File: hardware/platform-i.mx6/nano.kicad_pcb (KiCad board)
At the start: 4 copper layers, 85 x 56 mm, 196 parts, among them J1 SD-104031, J10 TC2030-IDC, J11 Conn_01x05, J2 TAG_CONNECT_JTAG, J3 TC2030-IDC, J4 USB_C_Receptacle_USB2.0, J5 CAN, J6 UART5, J7 I2C4, J8 ECSPI4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

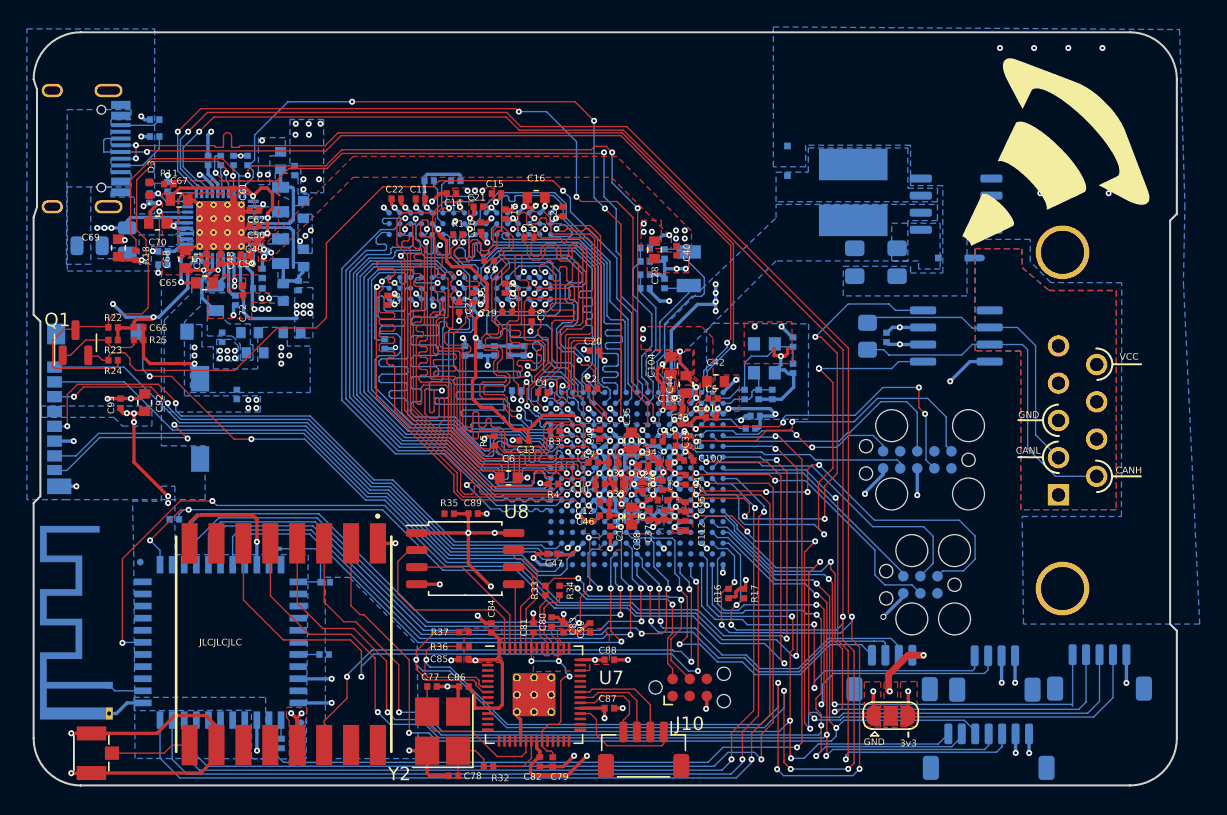
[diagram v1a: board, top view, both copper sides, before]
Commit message: Start reworking imx board into the new form factor
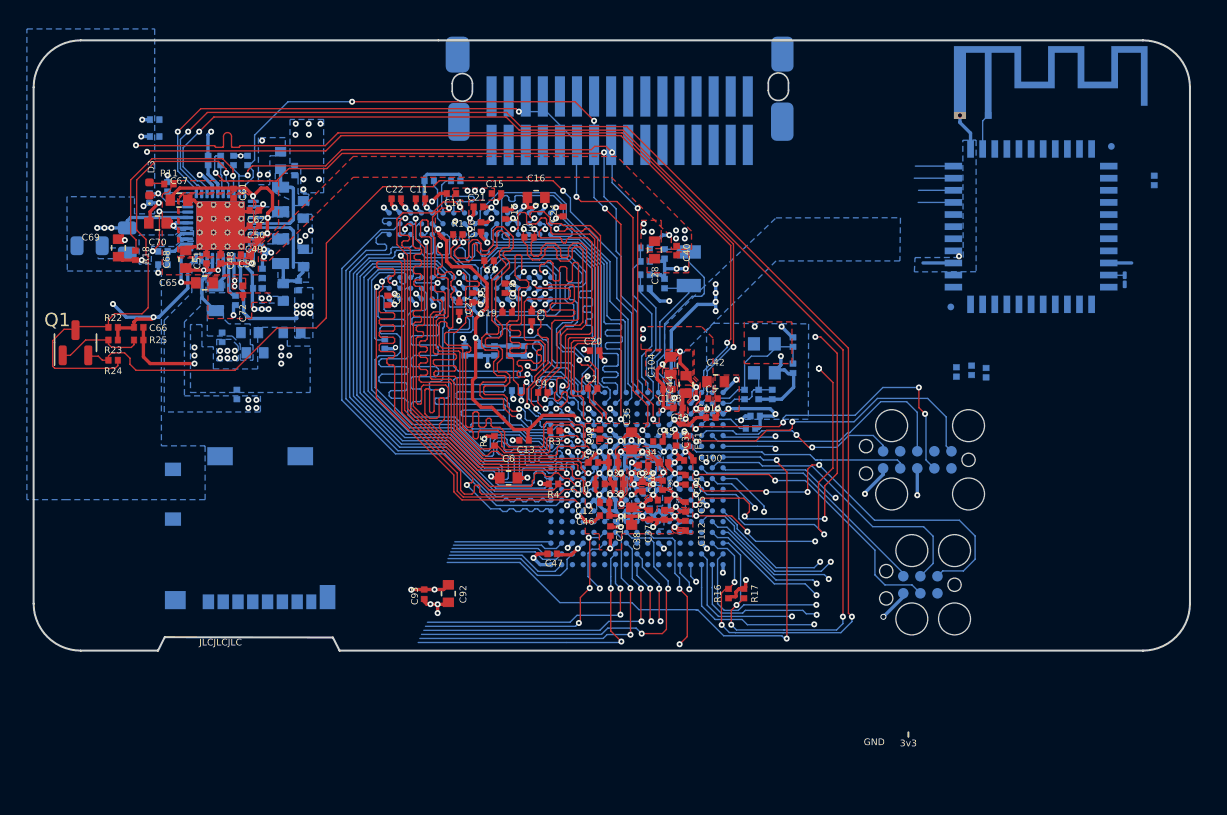
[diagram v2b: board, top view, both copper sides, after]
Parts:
- removed AE1: U.FL-R-SMT-1(10), ufl:HRS_U.FL-R-SMT-1(10)
- removed C73: 0.22uF, Custom Components:C_0402_narrow
- removed C75, C76: 10uF, Capacitor_SMD:C_0805_2012Metric_Pad1.18x1.45mm_HandSolder
- removed C77, C78: 10pF, Custom Components:C_0402_narrow
- removed C79, C81, C89: 1uF, Custom Components:C_0402_narrow
- removed C80, C82, C83, C84, C85, C86, C87, C88, C90: 0.1uF, Custom Components:C_0402_narrow
- removed D1, D2: D_Small, Diode_SMD:D_SOD-323F
- removed G***: LOGO, logos:cone
- removed J10: TC2030-IDC, Connector:Tag-Connect_TC2030-IDC-NL_2x03_P1.27mm_Vertical
- removed J11: Conn_01x05, Connector_JST:JST_SH_BM04B-SRSS-TB_1x04-1MP_P1.00mm_Vertical
- removed J4: USB_C_Receptacle_USB2.0, Connector_USB:USB_C_Receptacle_HRO_TYPE-C-31-M-12
- removed J5: CAN, Connector_Dsub:DSUB-9_Female_Horizontal_P2.77x2.84mm_EdgePinOffset4.94mm_Housed_MountingHolesOffset7.48mm
- removed J6: UART5, Connector_JST:JST_SH_BM05B-SRSS-TB_1x05-1MP_P1.00mm_Vertical
- removed J7: I2C4, Connector_JST:JST_SH_BM04B-SRSS-TB_1x04-1MP_P1.00mm_Vertical
- removed J8: ECSPI4, Connector_JST:JST_SH_BM07B-SRSS-TB_1x07-1MP_P1.00mm_Vertical
- removed J9: PWM, Connector_JST:JST_SH_BM04B-SRSS-TB_1x04-1MP_P1.00mm_Vertical
- removed JP1: IO_SW, Jumper:SolderJumper-3_P1.3mm_Open_RoundedPad1.0x1.5mm
- removed L5: 6.8uH, Inductor_SMD:L_Bourns_SRN6045TA
- removed R31: 120, Resistor_SMD:R_0805_2012Metric_Pad1.20x1.40mm_HandSolder
- removed R32, R35, R36, R37: 1k, Custom Components:R_0402_narrow
- removed R33, R34: 27.4, Custom Components:R_0402_narrow
- removed U3: TJA1051T, Package_SO:SOIC-8_3.9x4.9mm_P1.27mm
- removed U4: AP1509, Package_SO:SOP-8_3.9x4.9mm_P1.27mm
- removed U5: RFM69HCW, rfm69:XCVR_RFM69HW
- removed U7: RP2040, rp2040:RP2040-QFN-56
- removed U8: W25Q128JVS, Package_SO:SOIC-8_5.23x5.23mm_P1.27mm
- removed Y2: 12mhz, Crystal:Crystal_SMD_3225-4Pin_3.2x2.5mm_HandSoldering
- added J2: Conn_02x15_Odd_Even_Shielded, TE_DTM1312PA12PBR008:PinSocket_2x16_P1.27mm_Vertical_SMD, B.Cu at (63.6, 26.6)
- moved ANT1 77.9 mm to (91.0, 26.2), turned to 180 degrees
- moved R29 77.1 mm to (103.3, 31.0), turned to -90 degrees
- moved MOD1 67.7 mm to (94.2, 34.5), turned to -90 degrees
- moved L4 66.4 mm to (101.1, 38.4), turned to -90 degrees
- moved R28 57.3 mm to (88.6, 45.3)
- moved R30 52.6 mm to (89.7, 45.1), turned to 90 degrees
- moved C74 51.5 mm to (90.8, 45.3), turned to -90 degrees
- moved C92 26.7 mm to (50.8, 61.7)
- moved C93 26.7 mm to (49.0, 61.8)
- moved J1 20.8 mm to (36.1, 62.6), turned to 180 degrees
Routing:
- net GND: track 265.7 -> 174.4 mm, vias 143 -> 108
- net BT_WAKE: track 84.6 -> 3.98 mm, vias 4 -> 1
- net /IMX_Peripherals_1/TOUCH_SS0: track 87.3 -> 9.68 mm, vias 4 -> 1
- net DBG_GPIO0: track 76.7 -> 0.52 mm, vias 4 -> 1
- net /IMX_Peripherals_1/TOUCH_SCLK: track 84.2 -> 11.2 mm, vias 4 -> 1
- net /IMX_Peripherals_1/TOUCH_MISO: track 79.9 -> 8.53 mm, vias 3 -> 1
- net UART2_RTS: track 74.0 -> 3.38 mm, vias 2 -> 1
- net UART2_CTS: track 71.8 -> 3.20 mm, vias 2 -> 1
- net /IMX_Peripherals_1/TOUCH_MOSI: track 79.2 -> 10.6 mm, vias 4 -> 1
- net BT_RST: track 70.7 -> 3.97 mm, vias 2 -> 1
- net BOARD_SCL: track 163.3 -> 98.3 mm, vias 8 -> 4
- net BOARD_SDA: track 165.8 -> 101.0 mm, vias 8 -> 4
- net UART2_TXD: track 69.8 -> 7.23 mm, vias 2 -> 1
- net UART2_RXD: track 67.7 -> 6.71 mm, vias 2 -> 1
- net DCDC_3V3: track 81.3 -> 22.6 mm, vias 33 -> 18
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- removed copper zone on B.Cu, net /PMIC PF1550/BUCK_VIN
- removed copper zone on B.Cu, net Net-(D2-Pad1)
- removed copper zone on F.Cu, net Net-(J9-Pad4)
- removed copper zone on B.Cu, net OTG_VBUS
- removed copper zone on B.Cu, net VCC
- removed copper zone on F.Cu, net VCC
- removed copper zone on In1.Cu, net VCC
- removed copper zone on In2.Cu, net unconnected-(J4-PadS1)
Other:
- board size 85 x 56 mm -> 86 x 45.4 mm
- board text removed: "1. TOP SIGNAL 0.5oz/ft2"
- board text removed: "2. PWR 1oz/ft2"
- board text removed: "3. GND 1oz/ft2"
- board text removed: "4 Layer PCB stack up"
- board text removed: "4. BOTTOM SIGNAL 0.5oz/ft2"
- board text removed: "CANH"
- board text removed: "CANL"
- board text removed: "CAP 5V USB / GND"
- board text removed: "Designed by Connor Rigby https://github.com/ConnorRigby"
- board text removed: "GRID INCREMENT: 0.05 MILLIMITER"
- board text removed: "I.MX6 Development Board"
- board text removed: "I2C"
- board text removed: "MFG Rules Min track/spacing 4/4mil Min hole size 0.2mm 4 Layers Tenting vias"
- board text removed: "PWM"
- board text removed: "SPACE"
- board text removed: "SPI4"
- board text removed: "UART5"
- board text removed: "VCC"
- board text removed: "cts"
- board text removed: "gnd"
- board text removed: "miso"
- board text removed: "mosi"
- board text removed: "pwm1"
- board text removed: "pwm2"
- board text removed: "pwm4"
- board text removed: "rst"
- board text removed: "rts"
- board text removed: "rxd"
- board text removed: "scl"
- board text removed: "sclk"
- board text removed: "sda"
- board text removed: "ss0"
- board text removed: "txd"
